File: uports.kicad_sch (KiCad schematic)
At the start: 14 parts, among them J10 Conn_02x06_Odd_Even, J11 Conn_02x06_Odd_Even, J12 Conn_02x06_Odd_Even, J13 Conn_02x06_Odd_Even, J14 Conn_02x06_Odd_Even, J15 Conn_02x06_Odd_Even, J16 Conn_02x06_Odd_Even, J17 Conn_02x06_Odd_Even, J18 Conn_02x06_Odd_Even, J19 Conn_02x06_Odd_Even, J20 Conn_02x06_Odd_Even, J21 Conn_02x06_Odd_Even, J22 Conn_02x06_Odd_Even, J9 Conn_02x06_Odd_Even

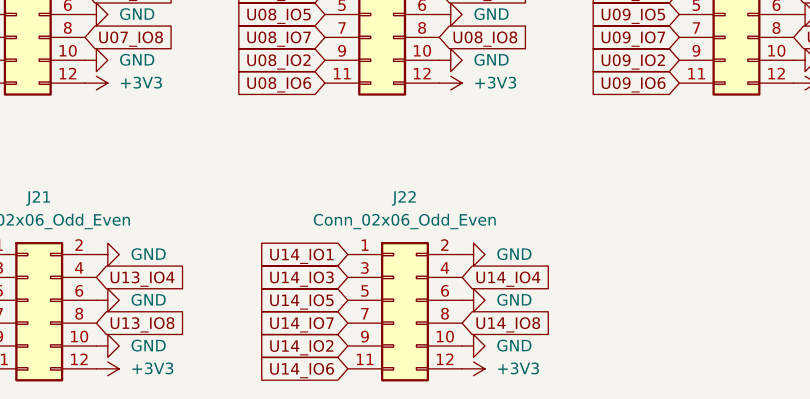
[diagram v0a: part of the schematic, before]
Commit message: added mount vias and start placement uports
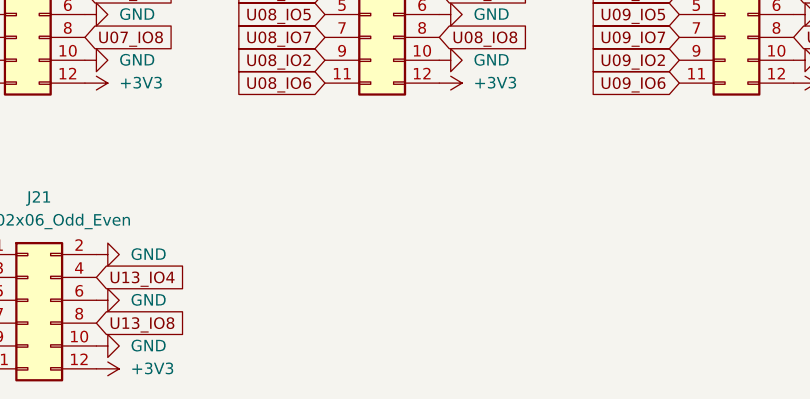
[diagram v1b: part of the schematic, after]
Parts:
- removed J22: Conn_02x06_Odd_Even, Connector_JST:JST_PHD_B12B-PHDSS_2x06_P2.00mm_Vertical, symbol Connector_Generic:Conn_02x06_Odd_Even
